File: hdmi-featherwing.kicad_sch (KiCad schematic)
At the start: 10 parts, among them J1 HDMI_A

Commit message: 0402 resistors
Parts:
- J1: LCSC C711354 -> (none)
- R1, R2, R3, R4, R5, R6, R7, R8: footprint Resistor_SMD:R_0805_2012Metric -> Resistor_SMD:R_0402_1005Metric; LCSC C17590 -> (none)
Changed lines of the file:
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@@
-(kicad_sch (version 20210126) (generator eeschema)
+(kicad_sch (version 20210406) (generator eeschema)
   (paper "A4")
   (junction (at 184.15 113.03) (diameter 0.9144) (color 0 0 0 0))
@@
     (property "Reference" "R1" (id 0) (at 153.035 60.96 90))
     (property "Value" "270" (id 1) (at 153.035 63.5 90))
-    (property "Footprint" "Resistor_SMD:R_0805_2012Metric" (id 2) (at 157.48 64.008 90)
+    (property "Footprint" "Resistor_SMD:R_0402_1005Metric" (id 2) (at 157.48 64.008 90)
       (effects (font (size 1.27 1.27)) hide)
     )
@@
       (effects (font (size 1.27 1.27)) hide)
     )
-    (property "LCSC" "C17590" (id 4) (at 157.48 62.23 90)
+    (property "LCSC" "" (id 4) (at 157.48 62.23 90)
       (effects (font (size 1.27 1.27)) hide)
     )
@@
     (property "Reference" "R2" (id 0) (at 153.035 66.04 90))
     (property "Value" "270" (id 1) (at 153.035 68.58 90))
-    (property "Footprint" "Resistor_SMD:R_0805_2012Metric" (id 2) (at 157.48 69.088 90)
+    (property "Footprint" "Resistor_SMD:R_0402_1005Metric" (id 2) (at 157.48 69.088 90)
       (effects (font (size 1.27 1.27)) hide)
     )
@@
       (effects (font (size 1.27 1.27)) hide)
     )
-    (property "LCSC" "C17590" (id 4) (at 157.48 67.31 90)
+    (property "LCSC" "" (id 4) (at 157.48 67.31 90)
       (effects (font (size 1.27 1.27)) hide)
     )
@@
     (property "Reference" "R3" (id 0) (at 153.035 71.12 90))
     (property "Value" "270" (id 1) (at 153.035 73.66 90))
-    (property "Footprint" "Resistor_SMD:R_0805_2012Metric" (id 2) (at 157.48 74.168 90)
+    (property "Footprint" "Resistor_SMD:R_0402_1005Metric" (id 2) (at 157.48 74.168 90)
       (effects (font (size 1.27 1.27)) hide)
     )
@@
       (effects (font (size 1.27 1.27)) hide)
     )
-    (property "LCSC" "C17590" (id 4) (at 157.48 72.39 90)
+    (property "LCSC" "" (id 4) (at 157.48 72.39 90)
       (effects (font (size 1.27 1.27)) hide)
     )
@@
     (property "Reference" "R4" (id 0) (at 153.035 76.2 90))
     (property "Value" "270" (id 1) (at 153.035 78.74 90))
-    (property "Footprint" "Resistor_SMD:R_0805_2012Metric" (id 2) (at 157.48 79.248 90)
+    (property "Footprint" "Resistor_SMD:R_0402_1005Metric" (id 2) (at 157.48 79.248 90)
       (effects (font (size 1.27 1.27)) hide)
     )
@@
       (effects (font (size 1.27 1.27)) hide)
     )
-    (property "LCSC" "C17590" (id 4) (at 157.48 77.47 90)
+    (property "LCSC" "" (id 4) (at 157.48 77.47 90)
       (effects (font (size 1.27 1.27)) hide)
     )
@@
     (property "Reference" "R5" (id 0) (at 169.545 63.5 90))
     (property "Value" "270" (id 1) (at 169.545 66.04 90))
-    (property "Footprint" "Resistor_SMD:R_0805_2012Metric" (id 2) (at 165.1 66.548 90)
+    (property "Footprint" "Resistor_SMD:R_0402_1005Metric" (id 2) (at 165.1 66.548 90)
       (effects (font (size 1.27 1.27)) hide)
     )
@@
       (effects (font (size 1.27 1.27)) hide)
     )
-    (property "LCSC" "C17590" (id 4) (at 165.1 64.77 90)
+    (property "LCSC" "" (id 4) (at 165.1 64.77 90)
       (effects (font (size 1.27 1.27)) hide)
     )
@@
     (property "Reference" "R6" (id 0) (at 169.545 68.58 90))
     (property "Value" "270" (id 1) (at 169.545 71.12 90))
-    (property "Footprint" "Resistor_SMD:R_0805_2012Metric" (id 2) (at 165.1 71.628 90)
+    (property "Footprint" "Resistor_SMD:R_0402_1005Metric" (id 2) (at 165.1 71.628 90)
       (effects (font (size 1.27 1.27)) hide)
     )
@@
       (effects (font (size 1.27 1.27)) hide)
     )
-    (property "LCSC" "C17590" (id 4) (at 165.1 69.85 90)
+    (property "LCSC" "" (id 4) (at 165.1 69.85 90)
       (effects (font (size 1.27 1.27)) hide)
     )
@@
     (property "Reference" "R7" (id 0) (at 169.545 73.66 90))
     (property "Value" "270" (id 1) (at 169.545 76.2 90))
-    (property "Footprint" "Resistor_SMD:R_0805_2012Metric" (id 2) (at 165.1 76.708 90)
+    (property "Footprint" "Resistor_SMD:R_0402_1005Metric" (id 2) (at 165.1 76.708 90)
       (effects (font (size 1.27 1.27)) hide)
     )
@@
       (effects (font (size 1.27 1.27)) hide)
     )
-    (property "LCSC" "C17590" (id 4) (at 165.1 74.93 90)
+    (property "LCSC" "" (id 4) (at 165.1 74.93 90)
       (effects (font (size 1.27 1.27)) hide)
     )
@@
     (property "Reference" "R8" (id 0) (at 169.545 78.74 90))
     (property "Value" "270" (id 1) (at 169.545 81.28 90))
-    (property "Footprint" "Resistor_SMD:R_0805_2012Metric" (id 2) (at 165.1 81.788 90)
+    (property "Footprint" "Resistor_SMD:R_0402_1005Metric" (id 2) (at 165.1 81.788 90)
       (effects (font (size 1.27 1.27)) hide)
     )
@@
       (effects (font (size 1.27 1.27)) hide)
     )
-    (property "LCSC" "C17590" (id 4) (at 165.1 80.01 90)
+    (property "LCSC" "" (id 4) (at 165.1 80.01 90)
       (effects (font (size 1.27 1.27)) hide)
     )
@@
       (effects (font (size 1.27 1.27)) hide)
     )
-    (property "LCSC" "C711354" (id 4) (at 186.69 82.55 0)
+    (property "LCSC" "" (id 4) (at 186.69 82.55 0)
       (effects (font (size 1.27 1.27)) hide)
     )
@@
     )
     (path "/12095942-e316-43e6-8e91-820591daa66e"
-      (reference "R1") (unit 1) (value "270") (footprint "Resistor_SMD:R_0805_2012Metric")
+      (reference "R1") (unit 1) (value "270") (footprint "Resistor_SMD:R_0402_1005Metric")
     )
     (path "/eeb927ea-8397-4c7d-9a56-27649363bfbf"
-      (reference "R2") (unit 1) (value "270") (footprint "Resistor_SMD:R_0805_2012Metric")
+      (reference "R2") (unit 1) (value "270") (footprint "Resistor_SMD:R_0402_1005Metric")
     )
     (path "/d3d37288-f0ba-4fe0-9fd0-56afc5bb6815"
-      (reference "R3") (unit 1) (value "270") (footprint "Resistor_SMD:R_0805_2012Metric")
+      (reference "R3") (unit 1) (value "270") (footprint "Resistor_SMD:R_0402_1005Metric")
     )
     (path "/c8b38ce0-8172-4ca5-b311-7991ef2356c2"
-      (reference "R4") (unit 1) (value "270") (footprint "Resistor_SMD:R_0805_2012Metric")
+      (reference "R4") (unit 1) (value "270") (footprint "Resistor_SMD:R_0402_1005Metric")
     )
     (path "/55298014-470c-4e6b-a6bd-6f35e8695295"
-      (reference "R5") (unit 1) (value "270") (footprint "Resistor_SMD:R_0805_2012Metric")
+      (reference "R5") (unit 1) (value "270") (footprint "Resistor_SMD:R_0402_1005Metric")
     )
     (path "/692d872f-84be-419d-83c1-adc9ca84bc76"
-      (reference "R6") (unit 1) (value "270") (footprint "Resistor_SMD:R_0805_2012Metric")
+      (reference "R6") (unit 1) (value "270") (footprint "Resistor_SMD:R_0402_1005Metric")
     )
     (path "/1725c309-b4c5-44b0-b5f8-36484d1f71d5"
-      (reference "R7") (unit 1) (value "270") (footprint "Resistor_SMD:R_0805_2012Metric")
+      (reference "R7") (unit 1) (value "270") (footprint "Resistor_SMD:R_0402_1005Metric")
     )
     (path "/f3c2cf24-508f-45aa-96e8-0cfa5e7c4c3d"
-      (reference "R8") (unit 1) (value "270") (footprint "Resistor_SMD:R_0805_2012Metric")
-    )
-  )
+      (reference "R8") (unit 1) (value "270") (footprint "Resistor_SMD:R_0402_1005Metric")
+    )
+  )

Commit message: use smt hdmi connector footprint
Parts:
- J1: footprint HDMI:HDMI-TH_HYC12-HDMIA19-61 -> HDMI:KH-HDMI-19P-Cu; LCSC (none) -> C709361
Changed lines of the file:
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@@
       (effects (font (size 1.27 1.27)) (justify left))
     )
-    (property "Footprint" "HDMI:HDMI-TH_HYC12-HDMIA19-61" (id 2) (at 187.325 82.55 0)
+    (property "Footprint" "HDMI:KH-HDMI-19P-Cu" (id 2) (at 187.325 82.55 0)
       (effects (font (size 1.27 1.27)) hide)
     )
@@
       (effects (font (size 1.27 1.27)) hide)
     )
-    (property "LCSC" "" (id 4) (at 186.69 82.55 0)
+    (property "LCSC" "C709361" (id 4) (at 186.69 82.55 0)
       (effects (font (size 1.27 1.27)) hide)
     )
@@
     )
     (path "/fe48d55d-272e-4f11-a1c3-2a9246c6f613"
-      (reference "J1") (unit 1) (value "HDMI_A") (footprint "HDMI:HDMI-TH_HYC12-HDMIA19-61")
+      (reference "J1") (unit 1) (value "HDMI_A") (footprint "HDMI:KH-HDMI-19P-Cu")
     )
     (path "/12095942-e316-43e6-8e91-820591daa66e"

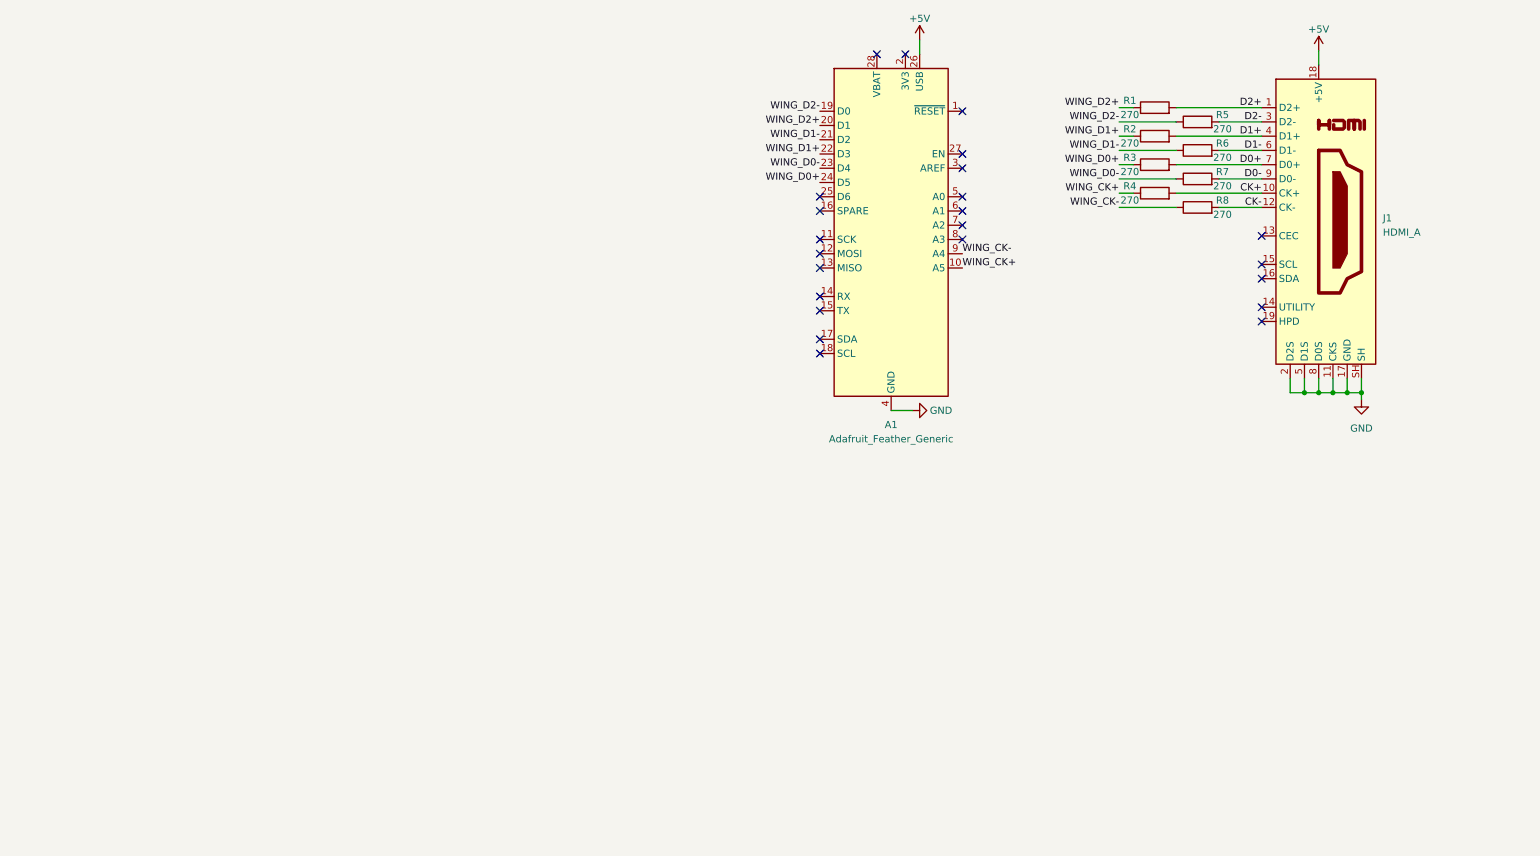
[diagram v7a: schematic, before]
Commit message: fix reference designators
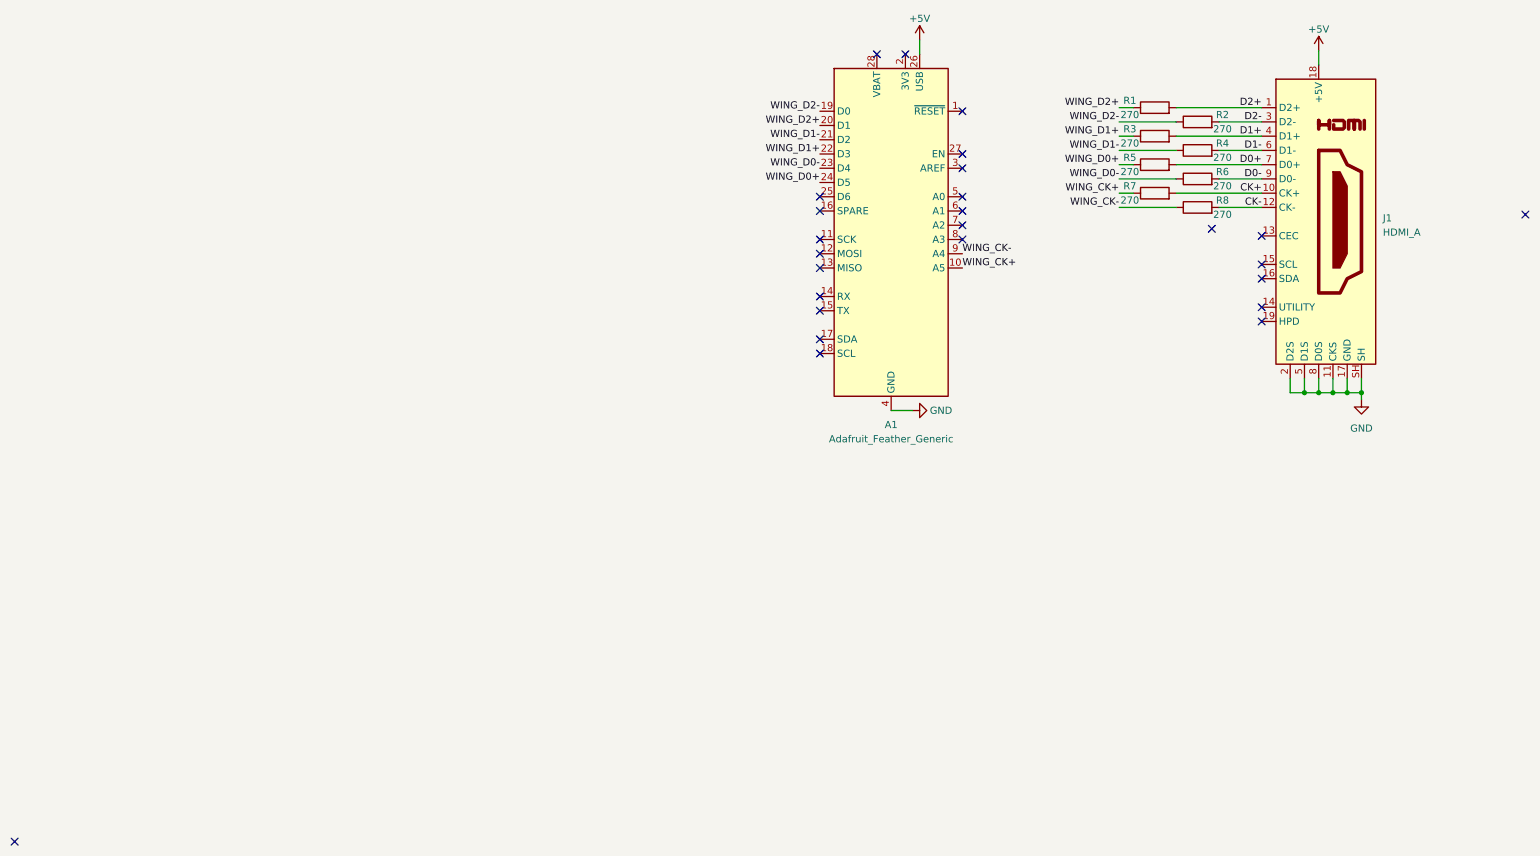
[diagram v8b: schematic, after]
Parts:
- renumbered R5 to R2, R2 to R3, R6 to R4, R3 to R5, R7 to R6, R4 to R7
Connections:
- no-connect marks 23 -> 26
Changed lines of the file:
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@@
   (junction (at 191.77 113.03) (diameter 0.9144) (color 0 0 0 0))
   (junction (at 194.31 113.03) (diameter 0.9144) (color 0 0 0 0))
+  (no_connect (at -45.72 193.04))
   (no_connect (at 97.79 78.105))
   (no_connect (at 97.79 80.645))
@@
   (no_connect (at 123.19 83.185))
   (no_connect (at 123.19 85.725))
+  (no_connect (at 167.64 83.82))
   (no_connect (at 176.53 85.09))
   (no_connect (at 176.53 90.17))
@@
   (no_connect (at 176.53 97.79))
   (no_connect (at 176.53 100.33))
+  (no_connect (at 223.52 81.28))
   (wire (pts (xy 110.49 116.205) (xy 114.3 116.205))
     (stroke (width 0) (type solid) (color 0 0 0 0))
@@
   (symbol (lib_id "power:+5V") (at 115.57 50.165 0) (unit 1)
     (in_bom yes) (on_board yes)
-    (property "Reference" "#PWR0103" (id 0) (at 115.57 53.975 0)
+    (property "Reference" "#PWR01" (id 0) (at 115.57 53.975 0)
       (effects (font (size 1.27 1.27)) hide)
     )
@@
   (symbol (lib_id "power:+5V") (at 186.69 52.07 0) (unit 1)
     (in_bom yes) (on_board yes)
-    (property "Reference" "#PWR0101" (id 0) (at 186.69 55.88 0)
+    (property "Reference" "#PWR02" (id 0) (at 186.69 55.88 0)
       (effects (font (size 1.27 1.27)) hide)
     )
@@
   (symbol (lib_id "power:GND") (at 114.3 116.205 90) (unit 1)
     (in_bom yes) (on_board yes)
-    (property "Reference" "#PWR0104" (id 0) (at 120.65 116.205 0)
+    (property "Reference" "#PWR04" (id 0) (at 120.65 116.205 0)
       (effects (font (size 1.27 1.27)) hide)
     )
@@
   (symbol (lib_id "power:GND") (at 194.31 114.3 0) (unit 1)
     (in_bom yes) (on_board yes)
-    (property "Reference" "#PWR0102" (id 0) (at 194.31 120.65 0)
+    (property "Reference" "#PWR03" (id 0) (at 194.31 120.65 0)
       (effects (font (size 1.27 1.27)) hide)
     )
@@
   (symbol (lib_id "Device:R") (at 157.48 67.31 90) (unit 1)
     (in_bom yes) (on_board yes)
-    (property "Reference" "R2" (id 0) (at 153.035 66.04 90))
+    (property "Reference" "R3" (id 0) (at 153.035 66.04 90))
     (property "Value" "270" (id 1) (at 153.035 68.58 90))
     (property "Footprint" "Resistor_SMD:R_0402_1005Metric" (id 2) (at 157.48 69.088 90)
@@
   (symbol (lib_id "Device:R") (at 157.48 72.39 90) (unit 1)
     (in_bom yes) (on_board yes)
-    (property "Reference" "R3" (id 0) (at 153.035 71.12 90))
+    (property "Reference" "R5" (id 0) (at 153.035 71.12 90))
     (property "Value" "270" (id 1) (at 153.035 73.66 90))
     (property "Footprint" "Resistor_SMD:R_0402_1005Metric" (id 2) (at 157.48 74.168 90)
@@
   (symbol (lib_id "Device:R") (at 157.48 77.47 90) (unit 1)
     (in_bom yes) (on_board yes)
-    (property "Reference" "R4" (id 0) (at 153.035 76.2 90))
+    (property "Reference" "R7" (id 0) (at 153.035 76.2 90))
     (property "Value" "270" (id 1) (at 153.035 78.74 90))
     (property "Footprint" "Resistor_SMD:R_0402_1005Metric" (id 2) (at 157.48 79.248 90)
@@
   (symbol (lib_id "Device:R") (at 165.1 64.77 90) (unit 1)
     (in_bom yes) (on_board yes)
-    (property "Reference" "R5" (id 0) (at 169.545 63.5 90))
+    (property "Reference" "R2" (id 0) (at 169.545 63.5 90))
     (property "Value" "270" (id 1) (at 169.545 66.04 90))
     (property "Footprint" "Resistor_SMD:R_0402_1005Metric" (id 2) (at 165.1 66.548 90)
@@
   (symbol (lib_id "Device:R") (at 165.1 69.85 90) (unit 1)
     (in_bom yes) (on_board yes)
-    (property "Reference" "R6" (id 0) (at 169.545 68.58 90))
+    (property "Reference" "R4" (id 0) (at 169.545 68.58 90))
     (property "Value" "270" (id 1) (at 169.545 71.12 90))
     (property "Footprint" "Resistor_SMD:R_0402_1005Metric" (id 2) (at 165.1 71.628 90)
@@
   (symbol (lib_id "Device:R") (at 165.1 74.93 90) (unit 1)
     (in_bom yes) (on_board yes)
-    (property "Reference" "R7" (id 0) (at 169.545 73.66 90))
+    (property "Reference" "R6" (id 0) (at 169.545 73.66 90))
     (property "Value" "270" (id 1) (at 169.545 76.2 90))
     (property "Footprint" "Resistor_SMD:R_0402_1005Metric" (id 2) (at 165.1 76.708 90)
@@
   )
   (symbol_instances
+    (path "/d52b8875-3af5-4294-9341-e43ce4899b1c"
+      (reference "#PWR01") (unit 1) (value "+5V") (footprint "")
+    )
     (path "/9282f211-5e95-45d4-8a17-88ec7ba41158"
-      (reference "#PWR0101") (unit 1) (value "+5V") (footprint "")
+      (reference "#PWR02") (unit 1) (value "+5V") (footprint "")
     )
     (path "/35fdfb15-70bd-47d9-86c3-99d6eed8234f"
-      (reference "#PWR0102") (unit 1) (value "GND") (footprint "")
-    )
-    (path "/d52b8875-3af5-4294-9341-e43ce4899b1c"
-      (reference "#PWR0103") (unit 1) (value "+5V") (footprint "")
+      (reference "#PWR03") (unit 1) (value "GND") (footprint "")
     )
     (path "/5d8c55b9-d212-4840-abd2-fd7daa7e8e99"
-      (reference "#PWR0104") (unit 1) (value "GND") (footprint "")
+      (reference "#PWR04") (unit 1) (value "GND") (footprint "")
     )
     (path "/3e967f1b-54c7-4065-ae92-6c0121775b5f"
@@
       (reference "R1") (unit 1) (value "270") (footprint "Resistor_SMD:R_0402_1005Metric")
     )
+    (path "/55298014-470c-4e6b-a6bd-6f35e8695295"
+      (reference "R2") (unit 1) (value "270") (footprint "Resistor_SMD:R_0402_1005Metric")
+    )
     (path "/eeb927ea-8397-4c7d-9a56-27649363bfbf"
-      (reference "R2") (unit 1) (value "270") (footprint "Resistor_SMD:R_0402_1005Metric")
+      (reference "R3") (unit 1) (value "270") (footprint "Resistor_SMD:R_0402_1005Metric")
+    )
+    (path "/692d872f-84be-419d-83c1-adc9ca84bc76"
+      (reference "R4") (unit 1) (value "270") (footprint "Resistor_SMD:R_0402_1005Metric")
     )
     (path "/d3d37288-f0ba-4fe0-9fd0-56afc5bb6815"
-      (reference "R3") (unit 1) (value "270") (footprint "Resistor_SMD:R_0402_1005Metric")
+      (reference "R5") (unit 1) (value "270") (footprint "Resistor_SMD:R_0402_1005Metric")
+    )
+    (path "/1725c309-b4c5-44b0-b5f8-36484d1f71d5"
+      (reference "R6") (unit 1) (value "270") (footprint "Resistor_SMD:R_0402_1005Metric")
     )
     (path "/c8b38ce0-8172-4ca5-b311-7991ef2356c2"
-      (reference "R4") (unit 1) (value "270") (footprint "Resistor_SMD:R_0402_1005Metric")
-    )
-    (path "/55298014-470c-4e6b-a6bd-6f35e8695295"
-      (reference "R5") (unit 1) (value "270") (footprint "Resistor_SMD:R_0402_1005Metric")
-    )
-    (path "/692d872f-84be-419d-83c1-adc9ca84bc76"
-      (reference "R6") (unit 1) (value "270") (footprint "Resistor_SMD:R_0402_1005Metric")
-    )
-    (path "/1725c309-b4c5-44b0-b5f8-36484d1f71d5"
       (reference "R7") (unit 1) (value "270") (footprint "Resistor_SMD:R_0402_1005Metric")
     )
